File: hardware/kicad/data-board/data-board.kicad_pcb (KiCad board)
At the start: 4 copper layers, 120 x 90 mm, 144 parts, among them J1 3.3V LoRaWAN, J14 Conn_02x05_Odd_Even, J17 Molex 470531000, J2 3.3V SWARM, J3 BMS I2C, J4 5V, J5 USB_67298-4090, J6 12V, J7 USB_OTG, J8 Conn_01x04, SW1 Wake, U1 TPD4EUSB30, U10 RAK5146, U11 EMC2301-1-ACZL-TR, U12 Swarm_M138, U13 FSUSB42MUX, U14 74LVC1G07SE-7, U2 TPD4EUSB30, U3 MagJack-A70-112-331N126, U4 TPD4EUSB30, U5 74LVC1G07SE-7, U6 USB2514B_Bi, U7 AP2553W6, U8 PCF85063AT/AAZ, U9 74LVC1G07SE-7, Y1 24MHz, Y2 X32K768S301

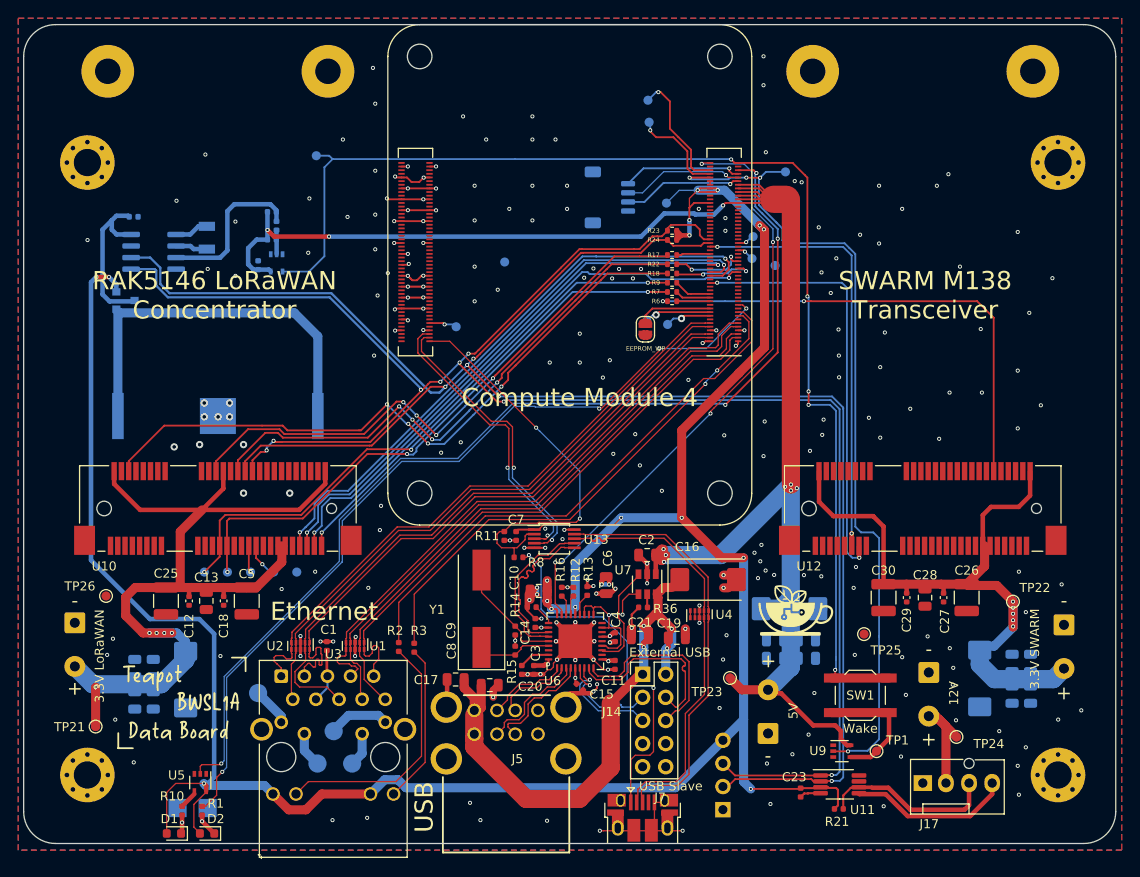
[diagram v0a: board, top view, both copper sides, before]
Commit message: fix incorrect fill rules
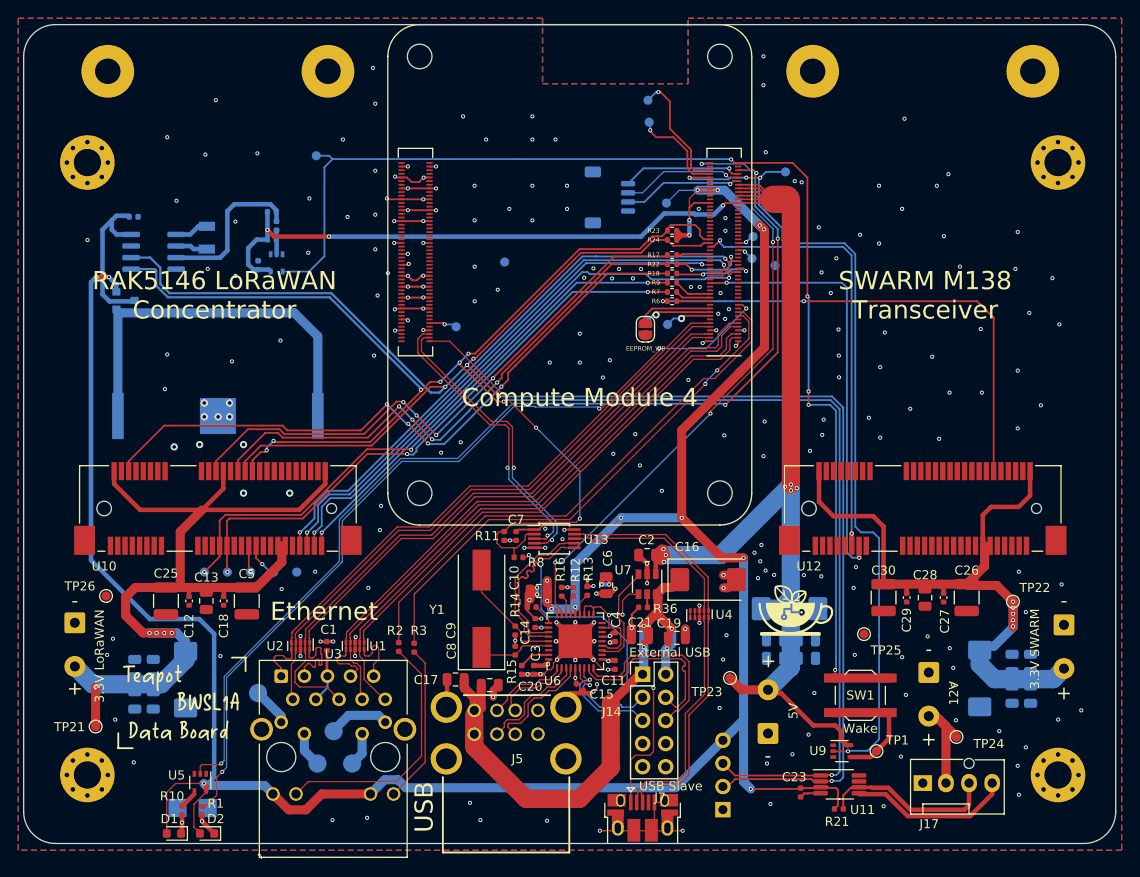
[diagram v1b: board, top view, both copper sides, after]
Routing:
- net /LORA_MOSI: track 59.9 -> 58.5 mm
- net /SWARM_RXD: track 47.9 -> 48.6 mm
- net GND: vias 234 -> 252

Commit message: fix fill rules
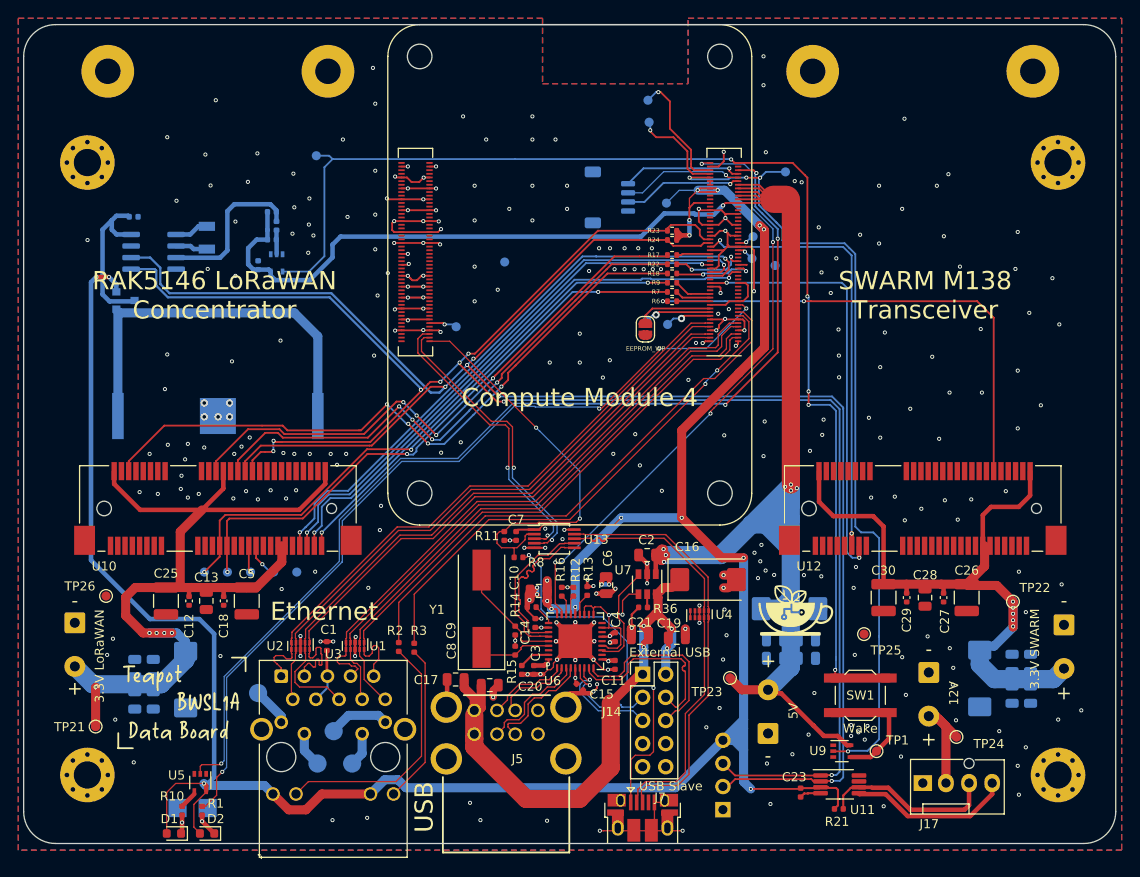
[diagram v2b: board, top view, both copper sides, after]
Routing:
- net GND: track 133.2 -> 198.9 mm, vias 252 -> 306
- net /+5v: track 185.2 -> 199.2 mm, vias 10 -> 8
- net /+3.3v: track 314.7 -> 319.1 mm
- net /LORA_CSN: track 59.9 -> 59.3 mm

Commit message: update hole to support solder standoff and decrease pogo pin contact hole size
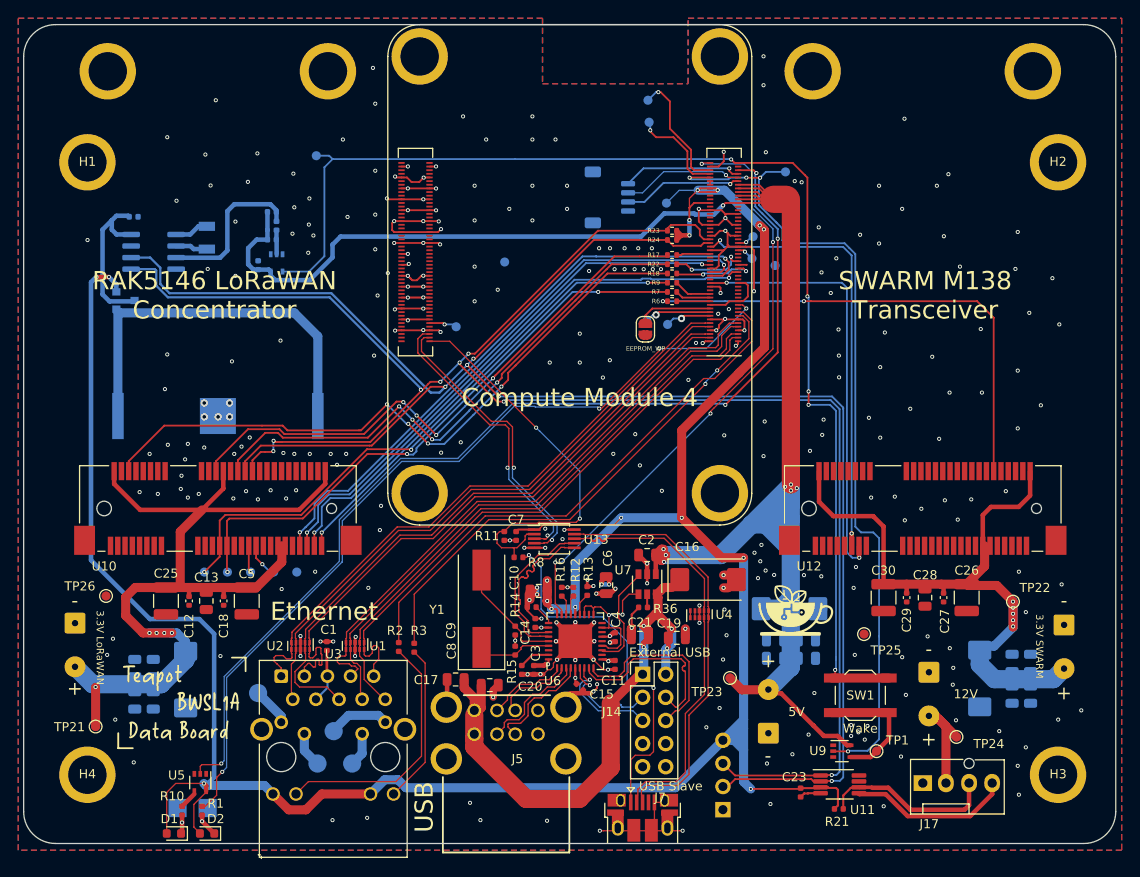
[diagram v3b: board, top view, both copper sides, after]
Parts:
- H1, H2, H3, H4: footprint MountingHole:MountingHole_3mm_Pad_Via -> Teapot:Sinhoo_SMTSO30
- J1, J2, J4, J6: footprint Connector_Wire:SolderWire-0.5sqmm_1x02_P4.8mm_D0.9mm_OD2.3mm -> Teapot:PogoPinContact_2_P4.8mm_D2.3mm_H0.7mm
- moved J1 2.40 mm to (90.4, 125.3)
- moved J4 2.40 mm to (167.2, 132.8)
- moved J2 2.37 mm to (199.1, 125.5)
- moved J6 2.34 mm to (184.3, 130.8)
